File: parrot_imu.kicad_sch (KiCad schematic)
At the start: 17 parts

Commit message: added tvs diodes to schematic
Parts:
- added D?: SMAJ24AQ-13-F, parrot_imu:SMAJ24AQ-13-F, symbol Device:D_Zener
- added U?: ESDCAN24-2BLY, SOT_24-2BLY_STM, symbol can_tvs:ESDCAN24-2BLY
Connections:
- net GND: now also D?.2 (A), U?.3
- net at C?.1, C?.1, J?.1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: now also D?.1 (K)
- net at J?.1, R?.1, U?.7 (CANH): now also U?.1
- net at J?.2, R?.2, U?.6 (CANL): now also U?.2
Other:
- note removed: "TVS Diodes (PEDISCAN)"
- moved on the sheet: C?, J?, R?, U?

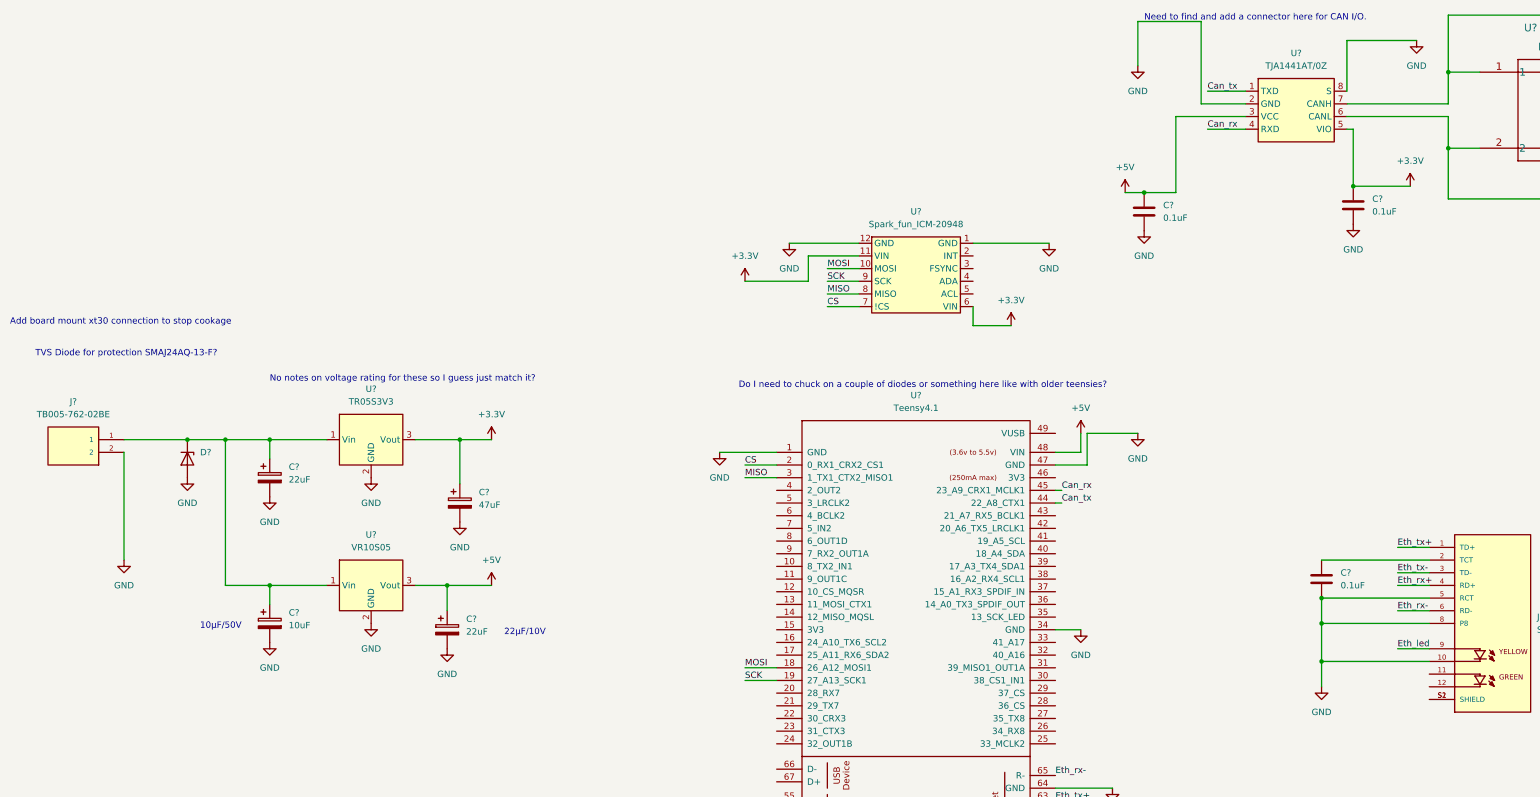
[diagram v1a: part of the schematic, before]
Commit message: switched to xt30 connector and added leds for power
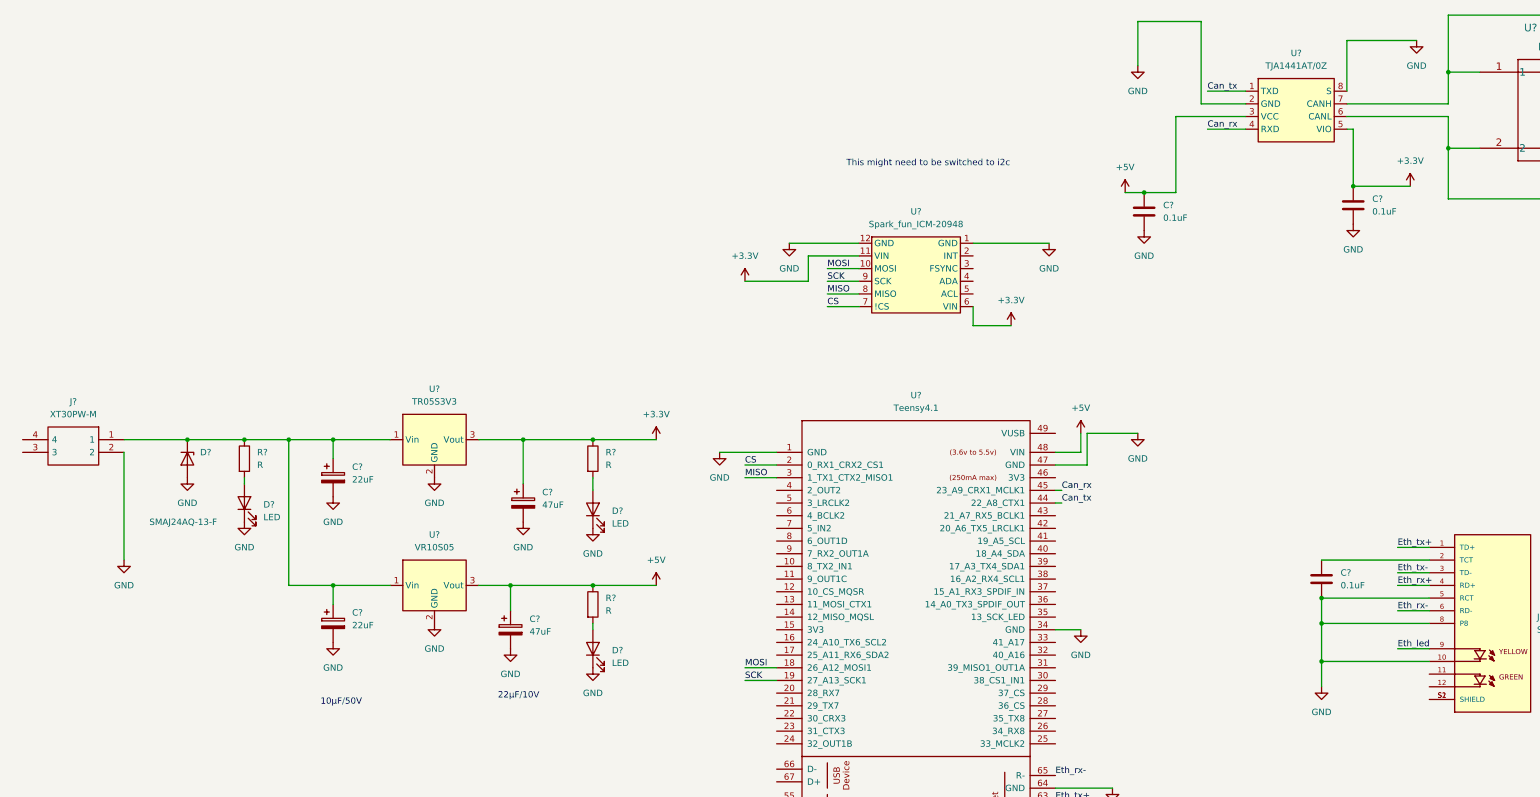
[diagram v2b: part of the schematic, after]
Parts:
- removed C?: 22uF, symbol Device:C_Polarized
- removed C?: 10uF, symbol Device:C_Polarized
- removed J?: TB005-762-02BE, connector_parrot:CUI_TB005-762-02BE, symbol connector_parrot:TB005-762-02BE
- added C?: 47uF, symbol Device:C_Polarized
- added C?: 22uF, symbol Device:C_Polarized
- added D? (x3): LED, symbol Device:LED
- added J?: XT30PW-M, XT30PWM, symbol connector_parrot:XT30PW-M
- added R? (x3): R, symbol Device:R
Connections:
- net +3.3V: now also R?.1
- net +5V: now also C?.1, R?.1
- net GND: now also C?.2, C?.2, D?.1 (K), D?.1 (K), D?.1 (K), J?.2
- net at C?.1, D?.1 (K), U?.1 (Vin)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: now also C?.1, J?.1, R?.1
- new net: D?.2 (A), R?.2 (x3)
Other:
- note added: "This might need to be switched to i2c"
- note removed: "Add board mount xt30 connection to stop cookage"
- note removed: "Do I need to chuck on a couple of diodes or something here like with older teensies?"
- note removed: "Need to find and add a connector here for CAN I/O."
- note removed: "No notes on voltage rating for these so I guess just match it?"
- note removed: "TVS Diode for protection SMAJ24AQ-13-F?"
- moved on the sheet: C?, U?

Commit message: filled in footprints and digikey id for most parts
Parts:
- removed C? (x2): 0.1uF, symbol Device:C
- removed C?: 47uF, symbol Device:C_Polarized
- removed C?: 22uF, symbol Device:C_Polarized
- removed D? (x2): LED, symbol Device:LED
- removed J?: XT30PW-M, XT30PWM, symbol connector_parrot:XT30PW-M
- removed R?: R, symbol Device:R
- removed R?: 60, symbol Device:R
- added C2: 22uF, Capacitor_THT:CP_Radial_D5.0mm_P2.00mm, symbol Device:C_Polarized
- added C3: 47uF, Capacitor_THT:CP_Radial_D6.3mm_P2.50mm, symbol Device:C_Polarized
- added C6, C7: 0.1uF, Capacitor_SMD:C_0603_1608Metric, symbol Device:C
- added D2, D4: LED, LED_SMD:LED_0603_1608Metric, symbol Device:LED
- added J1: Conn_01x02_Male, Connector_AMASS:AMASS_XT30PW-M_1x02_P2.50mm_Horizontal, symbol Connector:Conn_01x02_Male
- added R3: 1k, Resistor_SMD:R_0603_1608Metric, symbol Device:R
- added R4: 60, Resistor_SMD:R_0603_1608Metric, symbol Device:R
- C1: renamed from C?; footprint (none) -> Capacitor_THT:CP_Radial_D5.0mm_P2.00mm; Digikey (none) -> 732-8857-1-ND
- C4: renamed from C?; footprint (none) -> Capacitor_THT:CP_Radial_D6.3mm_P2.50mm; Digikey (none) -> 732-8859-1-ND
- C5: renamed from C?; footprint (none) -> Capacitor_SMD:C_0603_1608Metric; Digikey (none) -> 1276-1935-1-ND
- D3: renamed from D?; footprint (none) -> LED_SMD:LED_0603_1608Metric; Digikey (none) -> 3147-B1911USD-20D000114U1930CT-ND
- R1: renamed from R?; value R -> 10k; footprint (none) -> Resistor_SMD:R_0603_1608Metric; Digikey (none) -> RNCP0603FTD10K0CT-ND
- R2: renamed from R?; value R -> 1k; footprint (none) -> Resistor_SMD:R_0603_1608Metric; Digikey (none) -> RNCP0603FTD1K00CT-ND
- R5: renamed from R?; footprint (none) -> Resistor_SMD:R_0603_1608Metric; Digikey (none) -> 311-60.4HRCT-ND
- gave numbers to parts that had none: 9
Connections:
- net +3.3V: now also C7.1
- net +5V: now also C3.1, R3.1
- net GND: now also C2.2, C3.2, C6.2, C7.2, D2.1 (K), D4.1 (K), J1.1 (Pin_1), R4.2
- net at C1.1, D1.1 (K), R1.1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: now also C2.1, J1.2 (Pin_2)
- net at J3.1, U5.7 (CANH), U6.1: now also R4.1
- net at J2.2 (TCT): now also C6.1
- net at R1.2: now also D2.2 (A)
- new net: D4.2 (A), R3.2
- no-connect marks 0 -> 58
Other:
- note added: "Need to ad small pins to bom for ethernet"
- note removed: "10μF/50V"
- note removed: "22μF/10V"

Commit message: added missing footprint for can protection and imported parts to pcb design
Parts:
- U6: footprint SOT_24-2BLY_STM -> parrot_imu:ESDCAN24-2BLY
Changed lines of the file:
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@@
       (effects (font (size 1.524 1.524)))
     )
-    (property "Footprint" "SOT_24-2BLY_STM" (id 2) (at 331.47 49.784 0)
+    (property "Footprint" "parrot_imu:ESDCAN24-2BLY" (id 2) (at 331.47 49.784 0)
       (effects (font (size 1.524 1.524)) hide)
     )
@@
     )
     (path "/2fe48c89-8136-4a74-adea-b9d7e84b82b1"
-      (reference "U6") (unit 1) (value "ESDCAN24-2BLY") (footprint "SOT_24-2BLY_STM")
-    )
-  )
+      (reference "U6") (unit 1) (value "ESDCAN24-2BLY") (footprint "parrot_imu:ESDCAN24-2BLY")
+    )
+  )

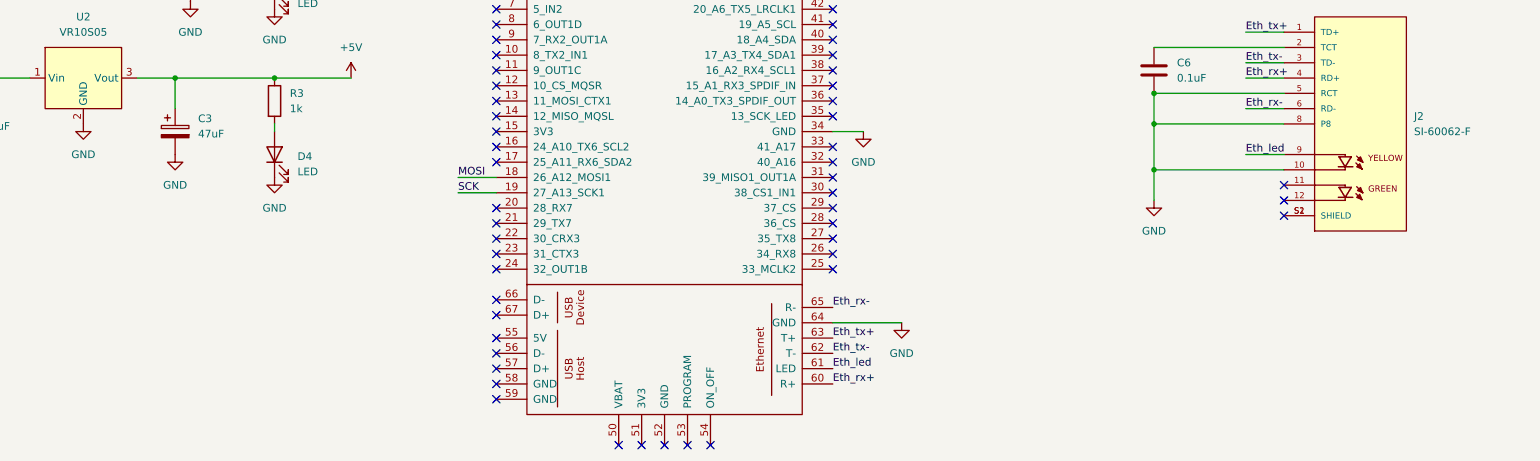
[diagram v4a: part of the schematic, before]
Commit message: sort out errors with footprints and add mounting holes
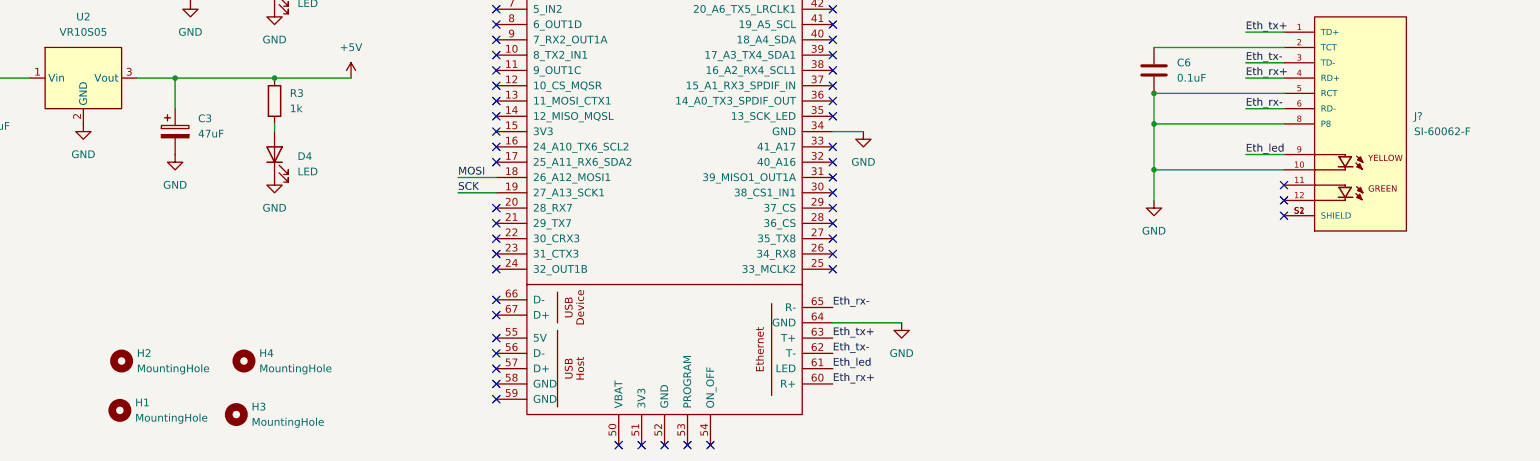
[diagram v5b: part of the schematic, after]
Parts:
- removed J2: SI-60062-F, Connector_RJ:RJ45_Bel_SI-60062-F, symbol SI-60062-F:SI-60062-F
- added H1, H2, H3, H4: MountingHole, MountingHole:MountingHole_3.2mm_M3, symbol Mechanical:MountingHole
- added J?: SI-60062-F, magjack:BEL_SI-60062-F, symbol SI-60062-F:SI-60062-F
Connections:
- net Eth_led: now also J?.9
- net Eth_rx+: now also J?.4 (RD+)
- net Eth_rx-: now also J?.6 (RD-)
- net Eth_tx+: now also J?.1 (TD+)
- net Eth_tx-: now also J?.3 (TD-)
- net GND: now also J?.10, J?.5 (RCT), J?.8 (P8)
- net at C6.1: now also J?.2 (TCT)
- new net: J?.S1 (SHIELD), J?.S2 (SHIELD)
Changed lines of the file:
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@@
     (pin "2")
+  )
+  (symbol (lib_id "SI-60062-F:SI-60062-F") (at 313.69 163.83 0) (unit 1)
+    (in_bom yes) (on_board yes) (fields_autoplaced)
+    (property "Reference" "J?" (id 0) (at 322.58 162.5599 0)
+      (effects (font (size 1.27 1.27)) (justify left))
+    )
+    (property "Value" "SI-60062-F" (id 1) (at 322.58 165.0999 0)
+      (effects (font (size 1.27 1.27)) (justify left))
+    )
+    (property "Footprint" "magjack:BEL_SI-60062-F" (id 2) (at 313.69 163.83 0)
+      (effects (font (size 1.27 1.27)) (justify bottom) hide)
+    )
+    (property "Datasheet" "" (id 3) (at 313.69 163.83 0)
+      (effects (font (size 1.27 1.27)) hide)
+    )
+    (property "STANDARD" "Manufacturer Recommendations" (id 4) (at 313.69 163.83 0)
+      (effects (font (size 1.27 1.27)) (justify bottom) hide)
+    )
+    (property "MAXIMUM_PACKAGE_HEIGHT" "15.21mm" (id 5) (at 313.69 163.83 0)
+      (effects (font (size 1.27 1.27)) (justify bottom) hide)
+    )
+    (property "MANUFACTURER" "Bel Fuse" (id 6) (at 313.69 163.83 0)
+      (effects (font (size 1.27 1.27)) (justify bottom) hide)
+    )
+    (property "PARTREV" "B0" (id 7) (at 313.69 163.83 0)
+      (effects (font (size 1.27 1.27)) (justify bottom) hide)
+    )
+    (pin "1")
+    (pin "10")
+    (pin "11")
+    (pin "12")
+    (pin "2")
+    (pin "3")
+    (pin "4")
+    (pin "5")
+    (pin "6")
+    (pin "8")
+    (pin "9")
+    (pin "S1")
+    (pin "S2")
   )
   (symbol (lib_id "power:GND") (at 63.5 143.51 0) (unit 1)
@@
     (pin "2")
   )
+  (symbol (lib_id "Mechanical:MountingHole") (at 127 212.09 0) (unit 1)
+    (in_bom yes) (on_board yes) (fields_autoplaced)
+    (property "Reference" "H3" (id 0) (at 129.54 210.8199 0)
+      (effects (font (size 1.27 1.27)) (justify left))
+    )
+    (property "Value" "MountingHole" (id 1) (at 129.54 213.3599 0)
+      (effects (font (size 1.27 1.27)) (justify left))
+    )
+    (property "Footprint" "MountingHole:MountingHole_3.2mm_M3" (id 2) (at 127 212.09 0)
+      (effects (font (size 1.27 1.27)) hide)
+    )
+    (property "Datasheet" "~" (id 3) (at 127 212.09 0)
+      (effects (font (size 1.27 1.27)) hide)
+    )
+  )
   (symbol (lib_id "power:GND") (at 243.84 85.09 0) (unit 1)
     (in_bom yes) (on_board yes) (fields_autoplaced)
@@
     (pin "2")
   )
+  (symbol (lib_id "Mechanical:MountingHole") (at 107.6596 211.397 0) (unit 1)
+    (in_bom yes) (on_board yes) (fields_autoplaced)
+    (property "Reference" "H1" (id 0) (at 110.1996 210.1269 0)
+      (effects (font (size 1.27 1.27)) (justify left))
+    )
+    (property "Value" "MountingHole" (id 1) (at 110.1996 212.6669 0)
+      (effects (font (size 1.27 1.27)) (justify left))
+    )
+    (property "Footprint" "MountingHole:MountingHole_3.2mm_M3" (id 2) (at 107.6596 211.397 0)
+      (effects (font (size 1.27 1.27)) hide)
+    )
+    (property "Datasheet" "~" (id 3) (at 107.6596 211.397 0)
+      (effects (font (size 1.27 1.27)) hide)
+    )
+  )
   (symbol (lib_id "power:GND") (at 224.79 87.63 0) (unit 1)
     (in_bom yes) (on_board yes) (fields_autoplaced)
@@
     )
     (pin "1")
+  )
+  (symbol (lib_id "Mechanical:MountingHole") (at 107.95 203.2 0) (unit 1)
+    (in_bom yes) (on_board yes) (fields_autoplaced)
+    (property "Reference" "H2" (id 0) (at 110.49 201.9299 0)
+      (effects (font (size 1.27 1.27)) (justify left))
+    )
+    (property "Value" "MountingHole" (id 1) (at 110.49 204.4699 0)
+      (effects (font (size 1.27 1.27)) (justify left))
+    )
+    (property "Footprint" "MountingHole:MountingHole_3.2mm_M3" (id 2) (at 107.95 203.2 0)
+      (effects (font (size 1.27 1.27)) hide)
+    )
+    (property "Datasheet" "~" (id 3) (at 107.95 203.2 0)
+      (effects (font (size 1.27 1.27)) hide)
+    )
   )
   (symbol (lib_id "power:GND") (at 355.6 60.96 0) (unit 1)
@@
     (pin "1")
   )
-  (symbol (lib_id "SI-60062-F:SI-60062-F") (at 313.69 163.83 0) (unit 1)
-    (in_bom yes) (on_board yes) (fields_autoplaced)
-    (property "Reference" "J2" (id 0) (at 322.58 162.5599 0)
-      (effects (font (size 1.27 1.27)) (justify left))
-    )
-    (property "Value" "SI-60062-F" (id 1) (at 322.58 165.0999 0)
-      (effects (font (size 1.27 1.27)) (justify left))
-    )
-    (property "Footprint" "Connector_RJ:RJ45_Bel_SI-60062-F" (id 2) (at 313.69 163.83 0)
-      (effects (font (size 1.27 1.27)) (justify bottom) hide)
-    )
-    (property "Datasheet" "" (id 3) (at 313.69 163.83 0)
-      (effects (font (size 1.27 1.27)) hide)
-    )
-    (property "STANDARD" "Manufacturer Recommendations" (id 4) (at 313.69 163.83 0)
-      (effects (font (size 1.27 1.27)) (justify bottom) hide)
-    )
-    (property "MAXIMUM_PACKAGE_HEIGHT" "15.21mm" (id 5) (at 313.69 163.83 0)
-      (effects (font (size 1.27 1.27)) (justify bottom) hide)
-    )
-    (property "MANUFACTURER" "Bel Fuse" (id 6) (at 313.69 163.83 0)
-      (effects (font (size 1.27 1.27)) (justify bottom) hide)
-    )
-    (property "PARTREV" "B0" (id 7) (at 313.69 163.83 0)
-      (effects (font (size 1.27 1.27)) (justify bottom) hide)
-    )
-    (property "Digikey" "507-SI-60062-F-ND" (id 8) (at 313.69 163.83 0)
-      (effects (font (size 1.27 1.27)) hide)
-    )
-    (pin "1")
-    (pin "10")
-    (pin "11")
-    (pin "12")
-    (pin "2")
-    (pin "3")
-    (pin "4")
-    (pin "5")
-    (pin "6")
-    (pin "8")
-    (pin "9")
-    (pin "S1")
-    (pin "S2")
-  )
   (symbol (lib_id "Device:R") (at 133.35 160.02 0) (unit 1)
     (in_bom yes) (on_board yes) (fields_autoplaced)
@@
     (pin "1")
     (pin "2")
+  )
+  (symbol (lib_id "Mechanical:MountingHole") (at 128.27 203.2 0) (unit 1)
+    (in_bom yes) (on_board yes) (fields_autoplaced)
+    (property "Reference" "H4" (id 0) (at 130.81 201.9299 0)
+      (effects (font (size 1.27 1.27)) (justify left))
+    )
+    (property "Value" "MountingHole" (id 1) (at 130.81 204.4699 0)
+      (effects (font (size 1.27 1.27)) (justify left))
+    )
+    (property "Footprint" "MountingHole:MountingHole_3.2mm_M3" (id 2) (at 128.27 203.2 0)
+      (effects (font (size 1.27 1.27)) hide)
+    )
+    (property "Datasheet" "~" (id 3) (at 128.27 203.2 0)
+      (effects (font (size 1.27 1.27)) hide)
+    )
   )
   (symbol (lib_id "parrot_imu:Spark_fun_ICM-20948") (at 198.12 93.98 0) (unit 1)
@@
       (reference "D4") (unit 1) (value "LED") (footprint "LED_SMD:LED_0603_1608Metric")
     )
+    (path "/56880c9d-0804-4594-9228-32c8db6eefc8"
+      (reference "H1") (unit 1) (value "MountingHole") (footprint "MountingHole:MountingHole_3.2mm_M3")
+    )
+    (path "/77a8828c-b669-412c-8364-99762d6a8a86"
+      (reference "H2") (unit 1) (value "MountingHole") (footprint "MountingHole:MountingHole_3.2mm_M3")
+    )
+    (path "/3c378538-e45f-409a-8fa5-70fe7ade792d"
+      (reference "H3") (unit 1) (value "MountingHole") (footprint "MountingHole:MountingHole_3.2mm_M3")
+    )
+    (path "/f65a4258-fa31-4a7c-8478-e5ac334451dd"
+      (reference "H4") (unit 1) (value "MountingHole") (footprint "MountingHole:MountingHole_3.2mm_M3")
+    )
     (path "/35ca6dd5-0fe6-4149-b1eb-072213388a9c"
       (reference "J1") (unit 1) (value "Conn_01x02_Male") (footprint "Connector_AMASS:AMASS_XT30PW-M_1x02_P2.50mm_Horizontal")
     )
-    (path "/ee96e4e8-cf28-4230-aa42-258281590056"
-      (reference "J2") (unit 1) (value "SI-60062-F") (footprint "Connector_RJ:RJ45_Bel_SI-60062-F")
-    )
     (path "/3048e5f9-287c-4759-b62e-bdb281c9ffef"
       (reference "J3") (unit 1) (value "TB005-762-02BE") (footprint "connector_parrot:CUI_TB005-762-02BE")
     )
+    (path "/0d20f8ee-a6f7-49a8-87a9-065aa3be88a2"
+      (reference "J?") (unit 1) (value "SI-60062-F") (footprint "magjack:BEL_SI-60062-F")
+    )
     (path "/b80ac4e5-0546-4f4a-ab29-51df51ca7732"
